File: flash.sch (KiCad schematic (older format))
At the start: 13 parts, among them U1 LFE5U-85F-6BG381C, U10 IS25LP128F-JBLE

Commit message: Adding default parts
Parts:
- D28, D29: footprint Diode_SMD:D_SOD-323_HandSoldering -> Diode_SMD:D_SOD-323
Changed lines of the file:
@@
 F 0 "D28" H 5000 3500 50  0000 C CNN
 F 1 "1N914" H 5400 3400 50  0000 C CNN
-F 2 "Diode_SMD:D_SOD-323_HandSoldering" H 5000 3400 50  0001 C CNN
+F 2 "Diode_SMD:D_SOD-323" H 5000 3400 50  0001 C CNN
 F 3 "~" H 5000 3400 50  0001 C CNN
 F 4 "Leave empty" H 5000 3400 50  0001 C CNN "Note"
@@
 F 0 "D29" H 5000 3450 50  0000 C CNN
 F 1 "1N914" H 5400 3550 50  0000 C CNN
-F 2 "Diode_SMD:D_SOD-323_HandSoldering" H 5000 3550 50  0001 C CNN
+F 2 "Diode_SMD:D_SOD-323" H 5000 3550 50  0001 C CNN
 F 3 "~" H 5000 3550 50  0001 C CNN
 	1    5000 3550

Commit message: Update
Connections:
- net labels added: LTDC_FROM_FPGA_HSYNC, LTDC_FROM_FPGA_VSYNC
- wire segments 28 -> 30
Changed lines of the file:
@@
 Text GLabel 8000 3800 2    60   Input ~ 0
 BTN_F2
-Text GLabel 8000 3900 2    60   Input ~ 0
-BTN_D
-Text GLabel 6500 3900 0    60   Input ~ 0
-BTN_L
 Text Notes 4700 1950 0    60   ~ 0
 pullups to allow entering USER mode\nTN1260: lattice ECP5 sysCONFIG guide p.6, p.8, p.13
@@
 Text Notes 4100 3300 0    60   ~ 0
 PWRBTn\non "power" sheet
+Text GLabel 8400 3250 2    60   Input ~ 0
+LTDC_FROM_FPGA_HSYNC
+Text GLabel 8000 3900 2    60   Input ~ 0
+BTN_D
+Text GLabel 6500 3900 0    60   Input ~ 0
+BTN_L
+Text GLabel 8400 3150 2    60   Input ~ 0
+LTDC_FROM_FPGA_VSYNC
+Text GLabel 8300 3250 0    60   Input ~ 0
+BTN_L
+Text GLabel 8300 3150 0    60   Input ~ 0
+BTN_D
+Wire Wire Line
+	8300 3150 8400 3150
+Wire Wire Line
+	8400 3250 8300 3250
 $EndSCHEMATC

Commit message: better RGB-OUT
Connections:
- net labels added: LTDC_FROM_FPGA_B4, LTDC_FROM_FPGA_B7
- net labels removed: BTN_F1, BTN_F2
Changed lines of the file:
@@
 	0    1    1    0
 $EndComp
-Text GLabel 6500 3800 0    60   Input ~ 0
-BTN_F1
-Text GLabel 8000 3800 2    60   Input ~ 0
-BTN_F2
 Text Notes 4700 1950 0    60   ~ 0
 pullups to allow entering USER mode\nTN1260: lattice ECP5 sysCONFIG guide p.6, p.8, p.13
@@
 Wire Wire Line
 	8400 3250 8300 3250
+Text GLabel 6500 3800 0    60   Input ~ 0
+LTDC_FROM_FPGA_B4
+Text GLabel 8000 3800 2    60   Input ~ 0
+LTDC_FROM_FPGA_B7
 $EndSCHEMATC

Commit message: More fixes
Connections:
- net labels removed: BTN_D, BTN_L
- wire segments 30 -> 28
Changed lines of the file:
@@
 Text Notes 4100 3300 0    60   ~ 0
 PWRBTn\non "power" sheet
-Text GLabel 8400 3250 2    60   Input ~ 0
+Text GLabel 6500 3900 0    60   Input ~ 0
 LTDC_FROM_FPGA_HSYNC
 Text GLabel 8000 3900 2    60   Input ~ 0
-BTN_D
-Text GLabel 6500 3900 0    60   Input ~ 0
-BTN_L
-Text GLabel 8400 3150 2    60   Input ~ 0
 LTDC_FROM_FPGA_VSYNC
-Text GLabel 8300 3250 0    60   Input ~ 0
-BTN_L
-Text GLabel 8300 3150 0    60   Input ~ 0
-BTN_D
-Wire Wire Line
-	8300 3150 8400 3150
-Wire Wire Line
-	8400 3250 8300 3250
 Text GLabel 6500 3800 0    60   Input ~ 0
 LTDC_FROM_FPGA_B4

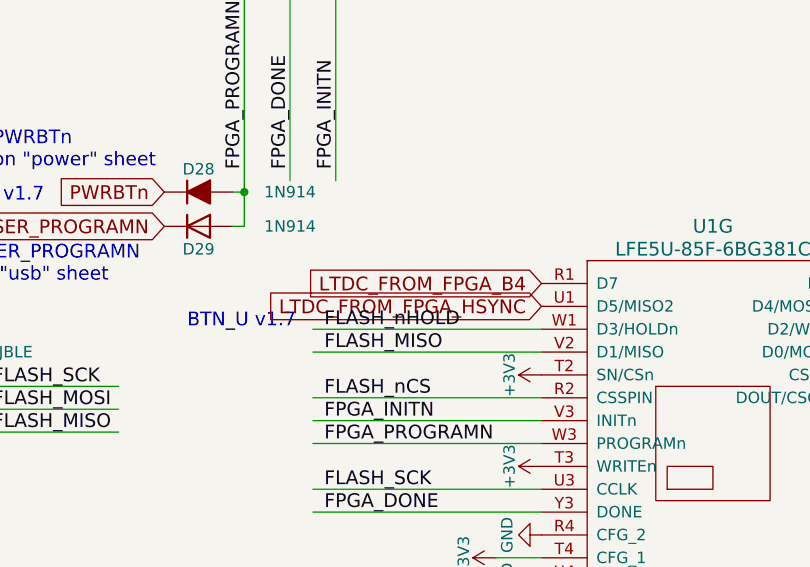
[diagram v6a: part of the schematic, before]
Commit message: Routing FPGA to LCD
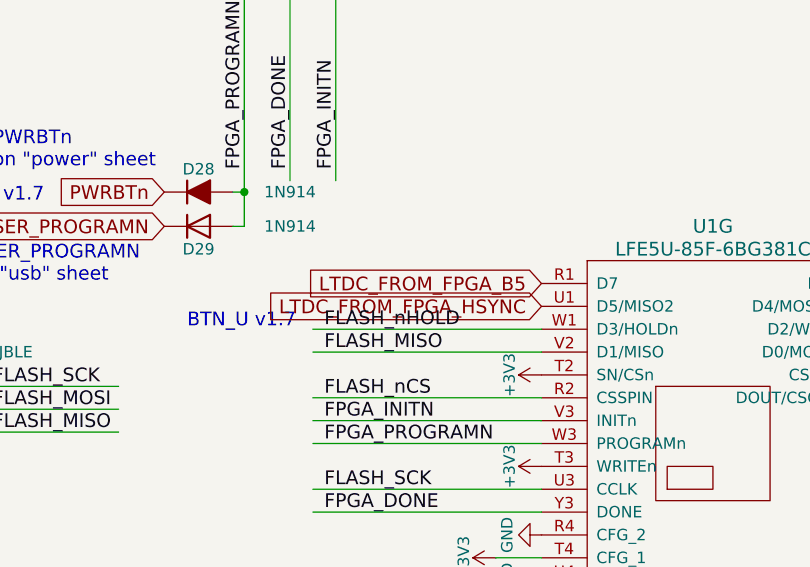
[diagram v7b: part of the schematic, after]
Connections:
- net labels added: LTDC_FROM_FPGA_B5
- net labels removed: LTDC_FROM_FPGA_B4
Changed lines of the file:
@@
 Text GLabel 8000 3900 2    60   Input ~ 0
 LTDC_FROM_FPGA_VSYNC
-Text GLabel 6500 3800 0    60   Input ~ 0
-LTDC_FROM_FPGA_B4
 Text GLabel 8000 3800 2    60   Input ~ 0
 LTDC_FROM_FPGA_B7
+Text GLabel 6500 3800 0    60   Input ~ 0
+LTDC_FROM_FPGA_B5
 $EndSCHEMATC
